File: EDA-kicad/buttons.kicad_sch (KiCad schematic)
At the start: 4 parts, among them SW4 PROG, SW5 VOL-, SW6 VOL+, SW7 POW

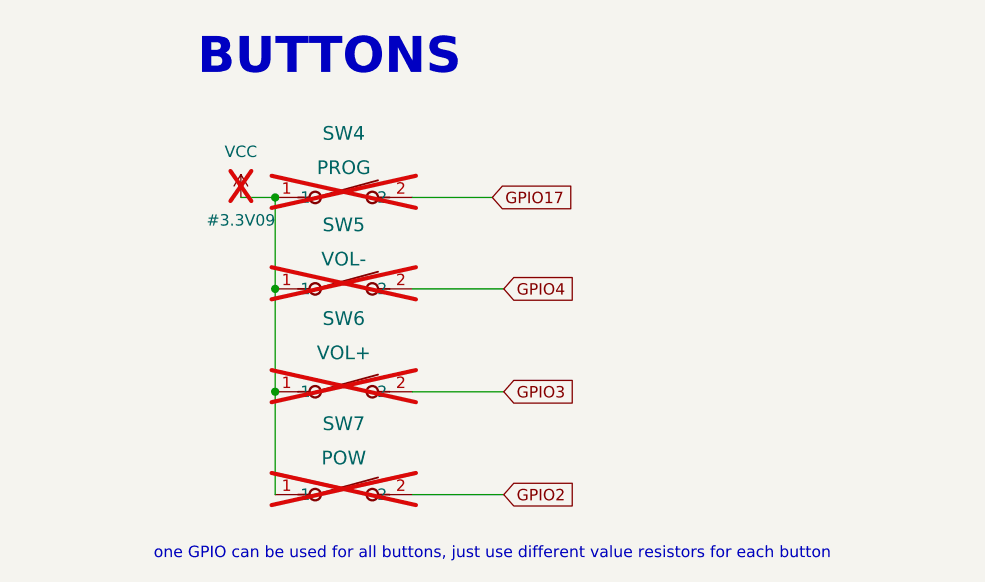
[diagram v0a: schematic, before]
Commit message: Improve KiCAD schematic design and labeling
- Replace overused global labels with hierarchical and local labels
- Add proper GND connections to components
- Fix BACKLIGHT- net issues
- Apply minor schematic fixes and cleanups
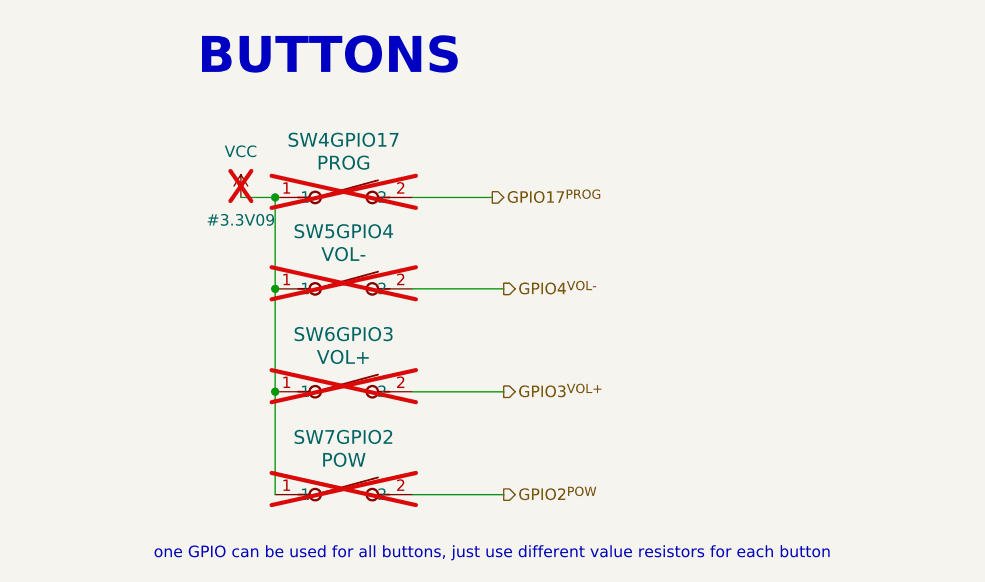
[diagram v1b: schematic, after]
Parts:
- renumbered SW4 to SW4GPIO17, SW5 to SW5GPIO4, SW6 to SW6GPIO3, SW7 to SW7GPIO2
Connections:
- net GPIO17 renamed GPIO17^{PROG}
- net GPIO2 renamed GPIO2^{POW}
- net GPIO3 renamed GPIO3^{VOL+}
- net GPIO4 renamed GPIO4^{VOL-}
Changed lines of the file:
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@@
 		)
 	)
-	(global_label "GPIO17"
-		(shape input)
-		(at 147.32 74.93 0)
-		(fields_autoplaced yes)
+	(hierarchical_label "GPIO2^{POW}"
+		(shape output)
+		(at 148.59 107.95 0)
 		(effects
 			(font
@@
 			(justify left)
 		)
-		(property "Intersheetrefs" "${INTERSHEET_REFS}"
-			(at 157.1995 74.93 0)
-			(effects
-				(font
-					(size 1.27 1.27)
-				)
-				(justify left)
-				(hide yes)
-			)
-		)
-	)
-	(global_label "GPIO3"
-		(shape input)
-		(at 148.59 96.52 0)
-		(fields_autoplaced yes)
+	)
+	(hierarchical_label "GPIO17^{PROG}"
+		(shape output)
+		(at 147.32 74.93 0)
 		(effects
 			(font
@@
 			(justify left)
 		)
-		(property "Intersheetrefs" "${INTERSHEET_REFS}"
-			(at 157.26 96.52 0)
-			(effects
-				(font
-					(size 1.27 1.27)
-				)
-				(justify left)
-				(hide yes)
-			)
-		)
-	)
-	(global_label "GPIO4"
-		(shape input)
-		(at 148.59 85.09 0)
-		(fields_autoplaced yes)
+	)
+	(hierarchical_label "GPIO3^{VOL+}"
+		(shape output)
+		(at 148.59 96.52 0)
 		(effects
 			(font
@@
 			(justify left)
 		)
-		(property "Intersheetrefs" "${INTERSHEET_REFS}"
-			(at 157.26 85.09 0)
-			(effects
-				(font
-					(size 1.27 1.27)
-				)
-				(justify left)
-				(hide yes)
-			)
-		)
-	)
-	(global_label "GPIO2"
-		(shape input)
-		(at 148.59 107.95 0)
-		(fields_autoplaced yes)
+	)
+	(hierarchical_label "GPIO4^{VOL-}"
+		(shape output)
+		(at 148.59 85.09 0)
 		(effects
 			(font
@@
 			(justify left)
 		)
-		(property "Intersheetrefs" "${INTERSHEET_REFS}"
-			(at 157.26 107.95 0)
-			(effects
-				(font
-					(size 1.27 1.27)
-				)
-				(justify left)
-				(hide yes)
-			)
-		)
 	)
 	(symbol
@@
 		(dnp yes)
 		(fields_autoplaced yes)
-		(property "Reference" "SW4"
-			(at 130.81 67.818 0)
+		(property "Reference" "SW4GPIO17"
+			(at 130.81 68.58 0)
 			(effects
 				(font
@@
 		)
 		(property "Value" "PROG"
-			(at 130.81 71.628 0)
+			(at 130.81 71.12 0)
 			(effects
 				(font
@@
 			(project "cm5-carrier"
 				(path "/28c5e4fe-1ec7-4477-97f0-d2ec1401fad5/7d72c53e-b066-4e49-bdb9-37372138f009"
-					(reference "SW4")
+					(reference "SW4GPIO17")
 					(unit 1)
 				)
@@
 		(dnp yes)
 		(fields_autoplaced yes)
-		(property "Reference" "SW6"
-			(at 130.81 88.392 0)
+		(property "Reference" "SW6GPIO3"
+			(at 130.81 90.17 0)
 			(effects
 				(font
@@
 		)
 		(property "Value" "VOL+"
-			(at 130.81 92.202 0)
+			(at 130.81 92.71 0)
 			(effects
 				(font
@@
 			(project "cm5-carrier"
 				(path "/28c5e4fe-1ec7-4477-97f0-d2ec1401fad5/7d72c53e-b066-4e49-bdb9-37372138f009"
-					(reference "SW6")
+					(reference "SW6GPIO3")
 					(unit 1)
 				)
@@
 		(dnp yes)
 		(fields_autoplaced yes)
-		(property "Reference" "SW5"
-			(at 130.81 77.978 0)
+		(property "Reference" "SW5GPIO4"
+			(at 130.81 78.74 0)
 			(effects
 				(font
@@
 		)
 		(property "Value" "VOL-"
-			(at 130.81 81.788 0)
+			(at 130.81 81.28 0)
 			(effects
 				(font
@@
 			(project "cm5-carrier"
 				(path "/28c5e4fe-1ec7-4477-97f0-d2ec1401fad5/7d72c53e-b066-4e49-bdb9-37372138f009"
-					(reference "SW5")
+					(reference "SW5GPIO4")
 					(unit 1)
 				)
@@
 		(dnp yes)
 		(fields_autoplaced yes)
-		(property "Reference" "SW7"
-			(at 130.81 100.076 0)
+		(property "Reference" "SW7GPIO2"
+			(at 130.81 101.6 0)
 			(effects
 				(font
@@
 		)
 		(property "Value" "POW"
-			(at 130.81 103.886 0)
+			(at 130.81 104.14 0)
 			(effects
 				(font
@@
 			(project "cm5-carrier"
 				(path "/28c5e4fe-1ec7-4477-97f0-d2ec1401fad5/7d72c53e-b066-4e49-bdb9-37372138f009"
-					(reference "SW7")
-					(unit 1)
-				)
+					(reference "SW7GPIO2")
+					(unit 1)
+				)
